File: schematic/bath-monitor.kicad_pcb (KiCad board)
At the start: 2 copper layers, 90 x 90 mm, 25 parts, among them J1 Conn_01x07, J2 Conn_01x04, SW1 Button_alice, SW2 Button_bob, SW3 Button_carol, SW4 Button_dave, SW5 Button_eve, U1 74AHCT1G125, U2 Pico2W

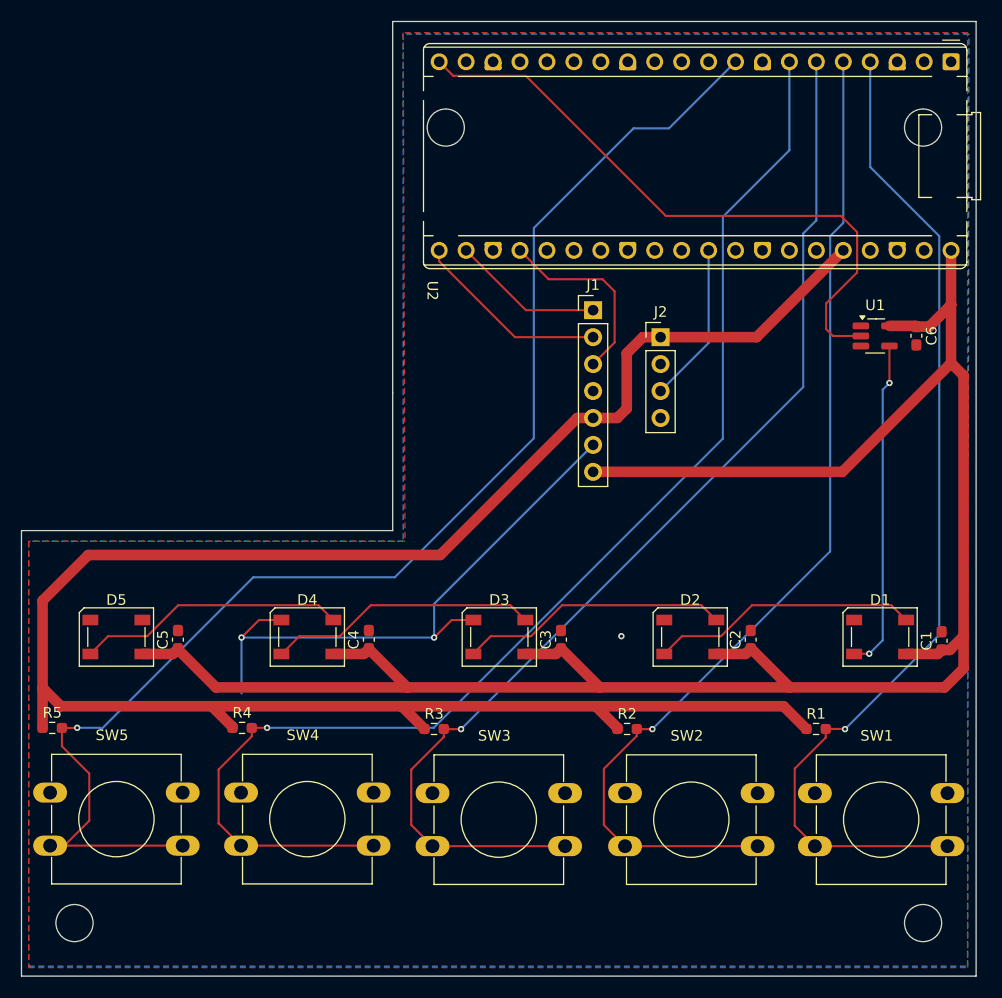
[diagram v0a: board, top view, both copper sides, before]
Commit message: 本体回路を作成し基板発注した
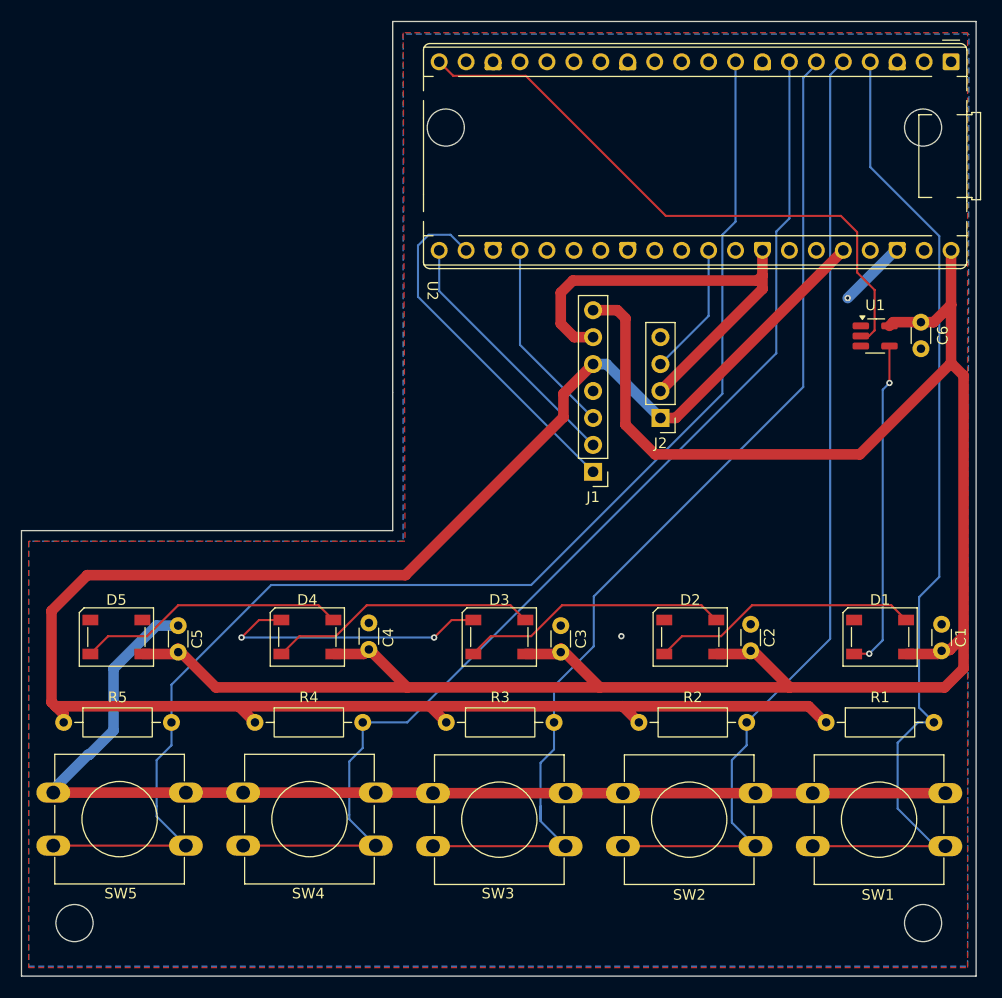
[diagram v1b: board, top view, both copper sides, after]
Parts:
- C1, C2, C3, C4, C5, C6: footprint Capacitor_SMD:C_0603_1608Metric_Pad1.08x0.95mm_HandSolder -> Capacitor_THT:C_Disc_D3.0mm_W1.6mm_P2.50mm
- R1, R2, R3, R4, R5: footprint Resistor_SMD:R_0603_1608Metric_Pad0.98x0.95mm_HandSolder -> Resistor_THT:R_Axial_DIN0207_L6.3mm_D2.5mm_P10.16mm_Horizontal
- moved J1 15.2 mm to (158.9, 97.5), turned to 180 degrees
- moved J2 7.62 mm to (165.2, 92.4), turned to 180 degrees
- moved C6 1.35 mm to (189.8, 83.3)
- moved R4 1.32 mm to (127.0, 121.1)
- moved R3 1.30 mm to (145.0, 121.1)
- moved R2 1.27 mm to (163.2, 121.1)
- moved R5 1.20 mm to (109.0, 121.1)
- moved C5 1.18 mm to (119.8, 114.5)
- moved C3 1.18 mm to (155.8, 114.5)
- moved R1 1.13 mm to (180.9, 121.1)
- moved C2 1.05 mm to (173.7, 114.3)
- moved C1 0.94 mm to (191.8, 114.3)
- moved C4 0.92 mm to (137.8, 114.2)
- moved SW5 0.30 mm to (108.0, 127.7)
- moved SW1 0.20 mm to (179.6, 127.8)
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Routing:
- net GND: track 56.6 -> 183.6 mm, vias 3 -> 4
- net Net-(J1-Pin_1): track 14.3 -> 33.7 mm
- net Net-(U2-GP5): track 119.6 -> 107.1 mm, vias 1 -> 0
- net +5V: track 196.7 -> 207.4 mm
- net Net-(J1-Pin_2): track 18.5 -> 24.4 mm
- net Net-(U2-GP3): track 97.5 -> 91.7 mm, vias 1 -> 0
- net Net-(U2-GP4): track 104.1 -> 99.8 mm, vias 1 -> 0
- net Net-(J2-Pin_3): track 15.1 -> 12.6 mm
- net Net-(U2-GP15): track 59.9 -> 57.5 mm
- net Net-(U2-GP6): track 128.2 -> 125.9 mm, vias 1 -> 0
- net +3V3: track 186.7 -> 185.0 mm
- net Net-(U2-GP2): track 96.7 -> 95.3 mm, vias 1 -> 0
